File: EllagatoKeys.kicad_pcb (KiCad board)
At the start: 2 copper layers, 88 x 32.5 mm, 23 parts, among them J1 Conn_01x10_Socket, SW1 SW_SPST, SW2 SW_SPST, SW3 SW_SPST, SW4 SW_SPST, SW5 RotaryEncoder_Switch_MP, U2 74AHCT1G125

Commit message: Production V1
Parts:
- removed J1: Conn_01x10_Socket, Connector_PinHeader_2.54mm:PinHeader_1x10_P2.54mm_Horizontal
- added C1: 100n, Capacitor_SMD:C_0805_2012Metric_Pad1.18x1.45mm_HandSolder, B.Cu at (110.2, 93.2)
- added J2: Conn_01x08_Socket, Connector_PinHeader_2.54mm:PinHeader_1x08_P2.54mm_Horizontal, F.Cu at (91.9, 78.6)
- added R1: 10k, Resistor_SMD:R_0805_2012Metric_Pad1.20x1.40mm_HandSolder, B.Cu at (96.2, 103.0)
- added TP0: Ground, TestPoint:TestPoint_Keystone_5010-5014_Multipurpose, F.Cu at (67.8, 103.8)
- added TP1: LED Data In, TestPoint:TestPoint_Keystone_5010-5014_Multipurpose, F.Cu at (142.8, 84.0)
- added TP2: REnc A, TestPoint:TestPoint_Keystone_5010-5014_Multipurpose, F.Cu at (130.8, 103.8)
- added TP3: REnc B, TestPoint:TestPoint_Keystone_5010-5014_Multipurpose, F.Cu at (135.8, 103.8)
- added TP4: SR PL, TestPoint:TestPoint_Keystone_5010-5014_Multipurpose, F.Cu at (75.2, 79.2)
- added TP5: SR CLK, TestPoint:TestPoint_Keystone_5010-5014_Multipurpose, F.Cu at (80.5, 79.5)
- added TP6: SR DATA, TestPoint:TestPoint_Keystone_5010-5014_Multipurpose, F.Cu at (85.8, 79.5)
- added U1: 74HC165, Package_SO:SOIC-16_3.9x9.9mm_P1.27mm, B.Cu at (104.0, 100.5)
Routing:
- net /SR_PL: track 0.00 -> 82.7 mm
- net /SR_CK: track 0.00 -> 64.9 mm
- net /Enc_B: track 37.9 -> 85.5 mm, vias 0 -> 1
- net /Enc_A: track 38.3 -> 77.8 mm, vias 0 -> 2
- net /SR_D: track 0.00 -> 32.2 mm
- net GND: track 0.00 -> 18.7 mm, vias 0 -> 1
- net /btn_C: track 21.0 -> 9.03 mm
- net /btn_OnOff: track 33.6 -> 24.3 mm, vias 0 -> 1
- net Net-(U1-D7): track 0.00 -> 8.74 mm
- net Net-(LED5-DIN): track 12.7 -> 20.5 mm
- net /Led_Input: track 12.2 -> 19.3 mm
- net /btn_B: track 28.7 -> 26.5 mm, vias 0 -> 1
- net /btn_A: track 41.6 -> 40.6 mm, vias 0 -> 1
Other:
- board text added: "CLK"
- board text added: "Data"
- board text added: "PL"
- board text removed: "Enc P"
- board text removed: "SW1"
- board text removed: "SW2"
- board text removed: "SW3"
- board text removed: "SW4"

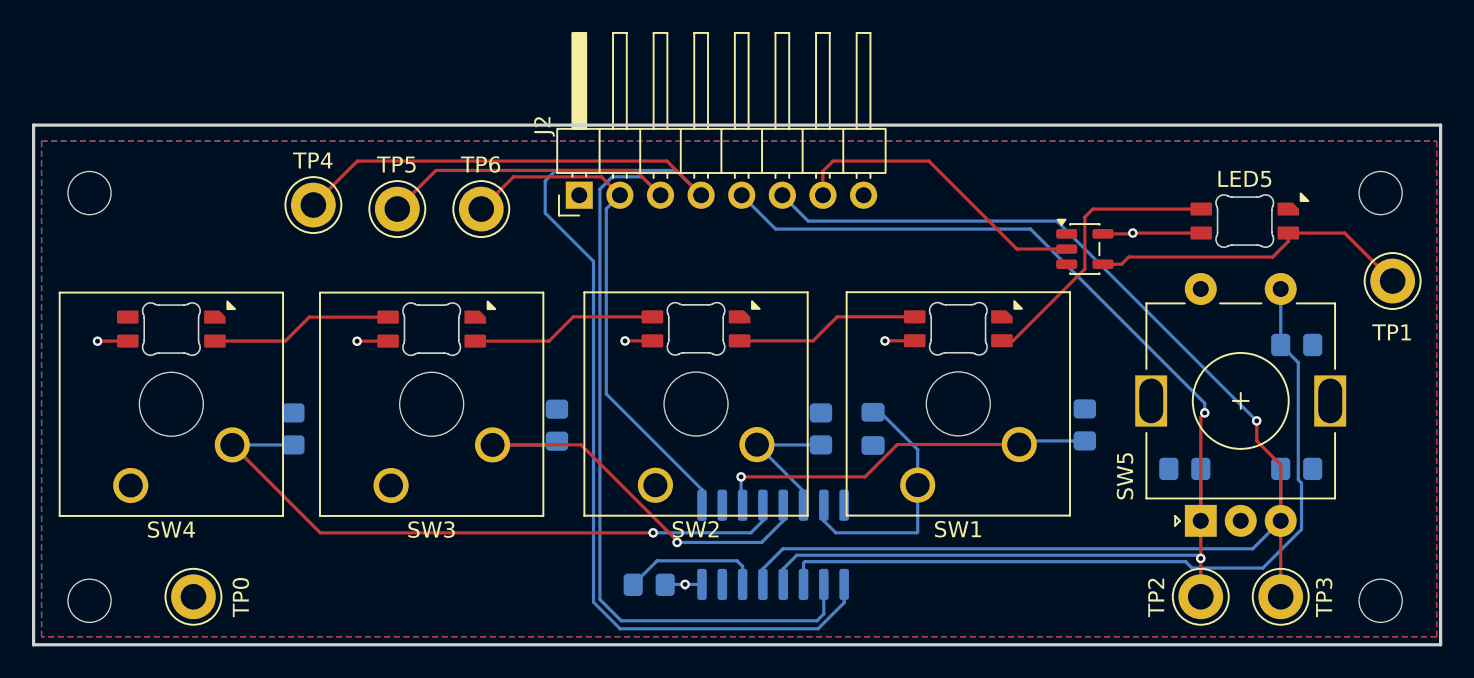
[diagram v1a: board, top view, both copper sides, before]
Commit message: +Added Decoupling Cap to LED !!Added connection to VCC for LED2&3 !Restored compoenent labels
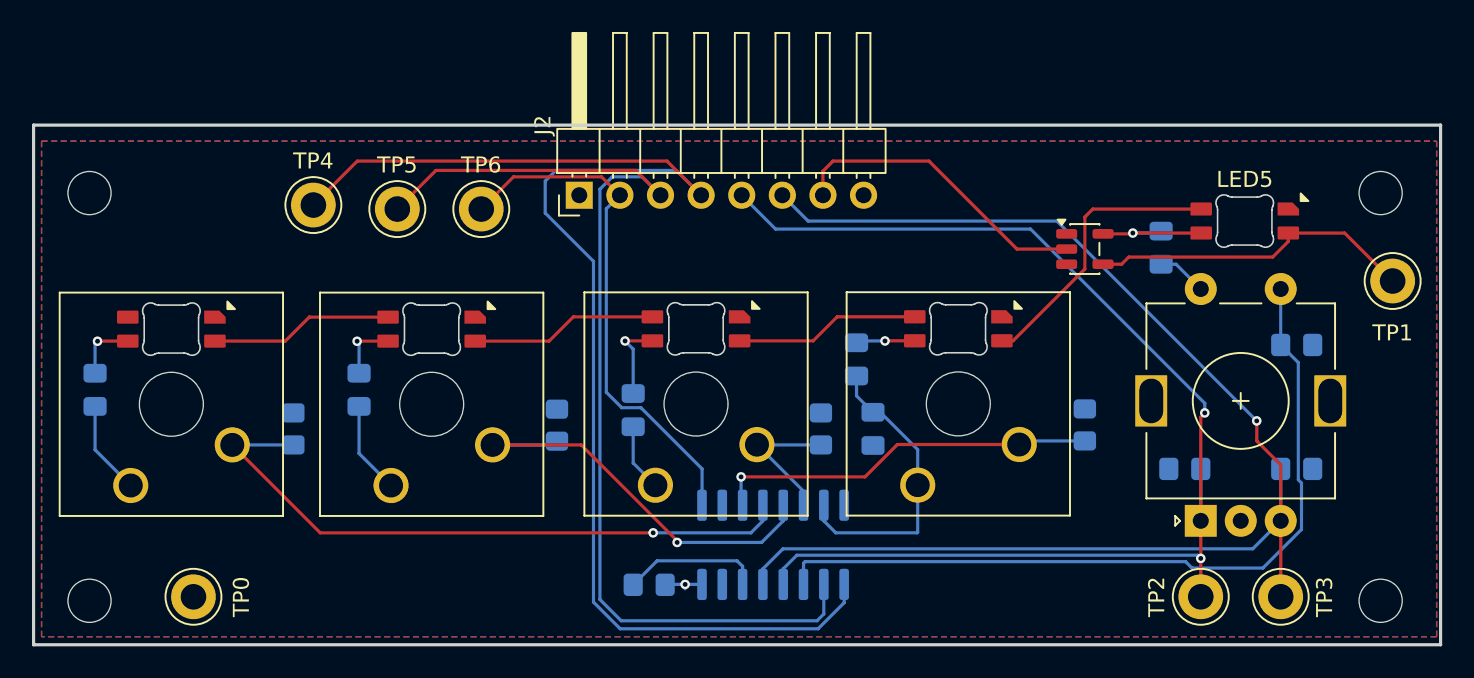
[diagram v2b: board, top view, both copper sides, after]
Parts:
- added C2: 100n, Capacitor_SMD:C_0805_2012Metric_Pad1.18x1.45mm_HandSolder, B.Cu at (61.6, 90.8)
- added C3: 100n, Capacitor_SMD:C_0805_2012Metric_Pad1.18x1.45mm_HandSolder, B.Cu at (78.1, 90.8)
- added C4: 100n, Capacitor_SMD:C_0805_2012Metric_Pad1.18x1.45mm_HandSolder, B.Cu at (95.2, 92.1)
- added C5: 100n, Capacitor_SMD:C_0805_2012Metric_Pad1.18x1.45mm_HandSolder, B.Cu at (109.2, 88.9)
- added C6: 100n, Capacitor_SMD:C_0805_2012Metric_Pad1.18x1.45mm_HandSolder, B.Cu at (128.3, 81.9)
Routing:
- net GND: track 18.7 -> 40.4 mm
- net +5V: track 13.6 -> 24.8 mm
- net /SR_D: track 32.2 -> 32.9 mm
